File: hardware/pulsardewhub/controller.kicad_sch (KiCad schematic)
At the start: 9 parts, among them J1 SWD, U1 STM32G0B1KBU6, U2 SHT40-AD1B-R2

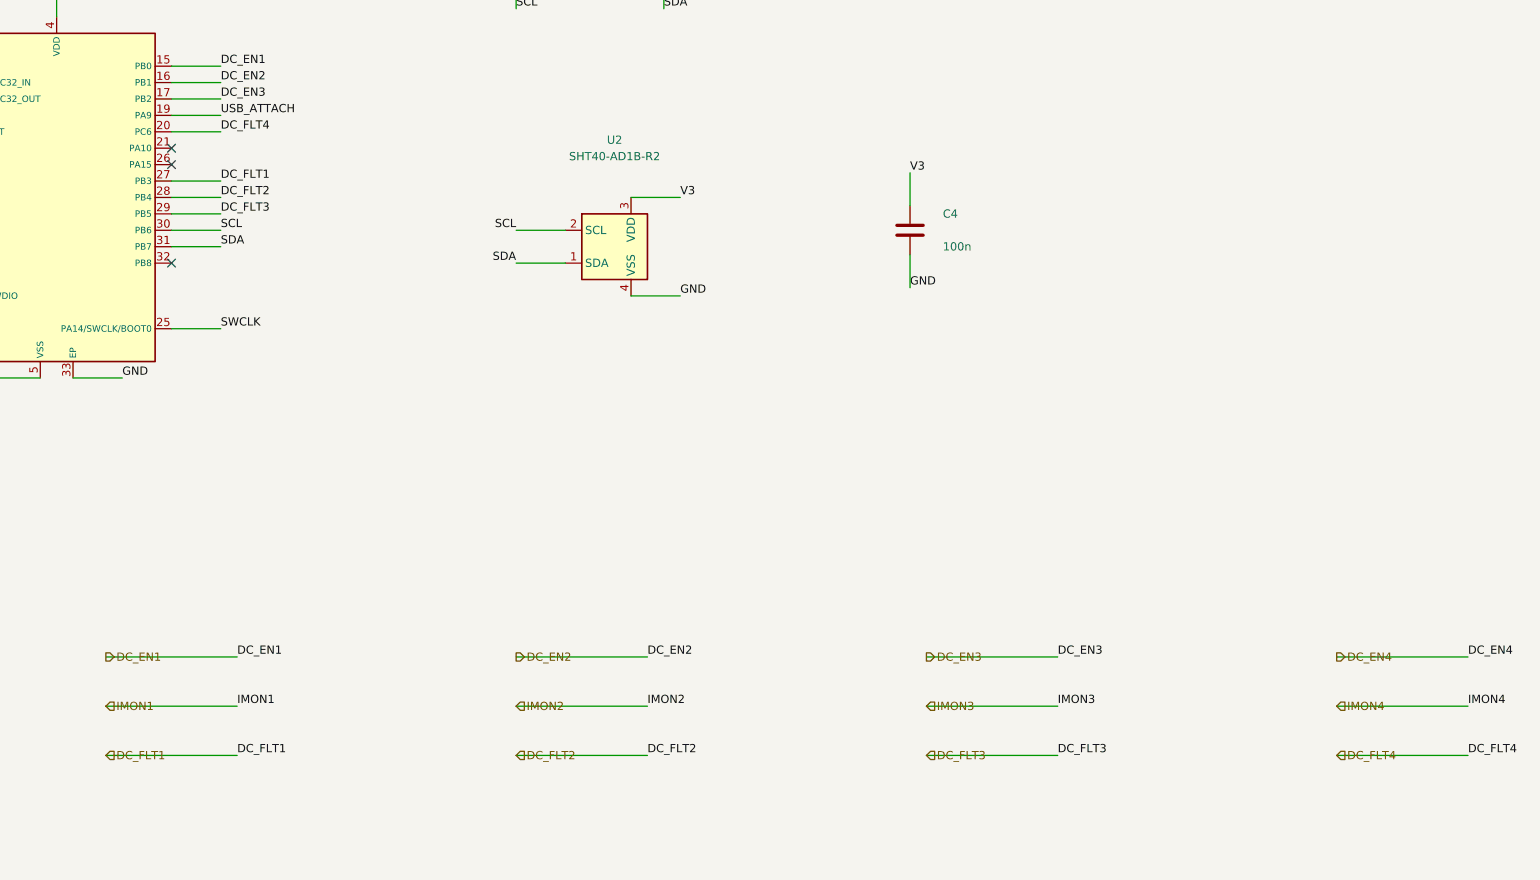
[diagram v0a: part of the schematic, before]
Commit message: Use TPS259827 high-side switches for 12–18 V DC outlets
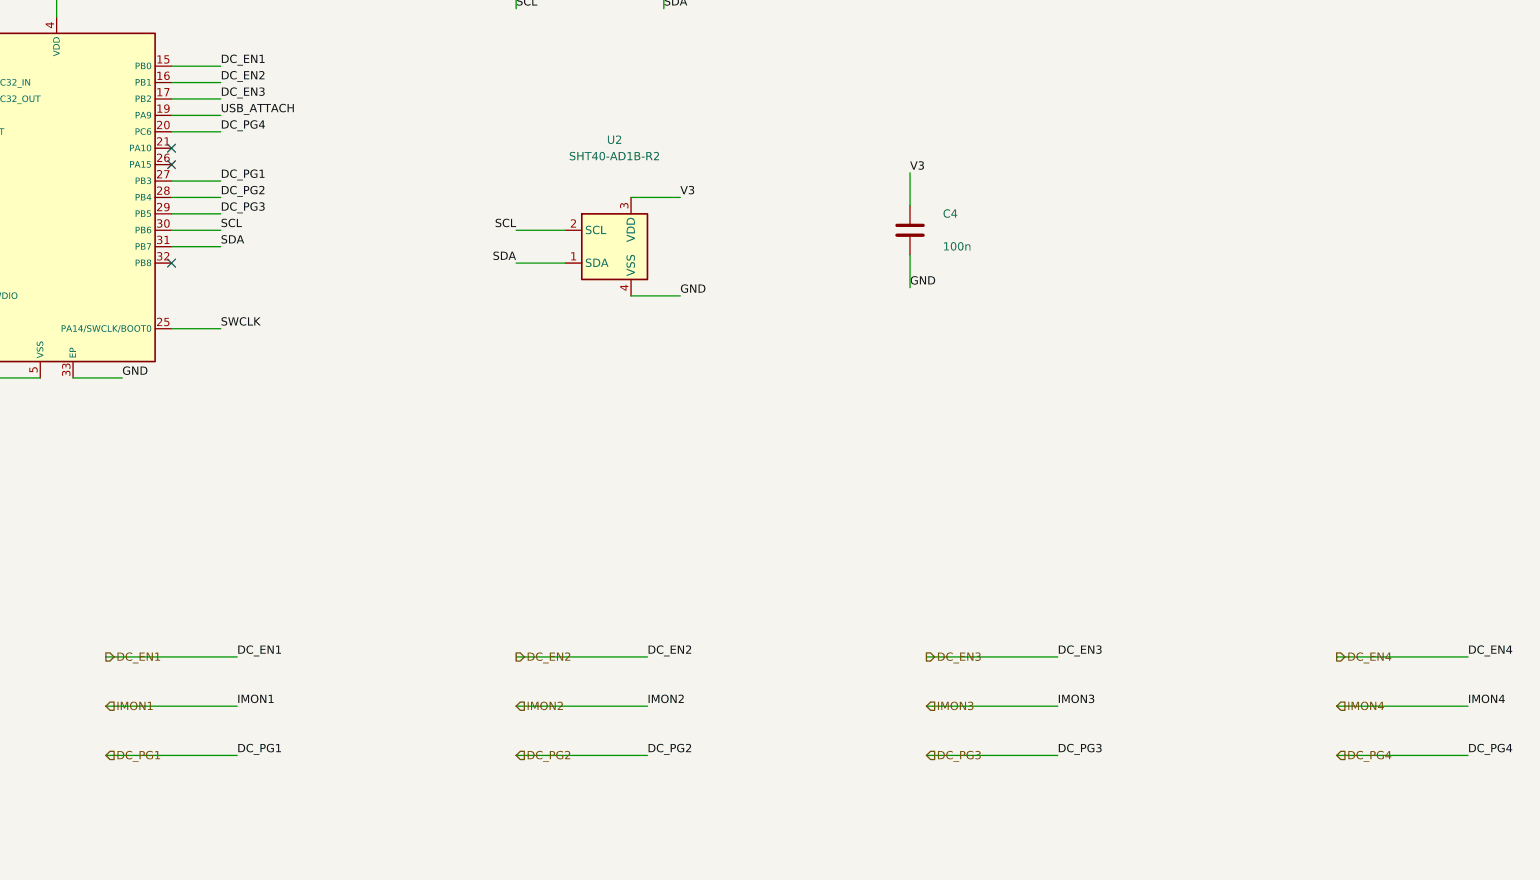
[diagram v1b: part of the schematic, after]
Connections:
- net DC_FLT1 renamed DC_PG1
- net DC_FLT2 renamed DC_PG2
- net DC_FLT3 renamed DC_PG3
- net DC_FLT4 renamed DC_PG4
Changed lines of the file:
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@@
 (kicad_sch (version 20260306) (generator "eeschema") (generator_version "10.0") (paper "A3")
-(title_block (title "PulsarDew Hub - STM32 controller and ambient sensor") (date "2026-10-03") (rev "0.1-draft") (company "PulsarFab"))
+(title_block (title "PulsarDew Hub - STM32 controller and ambient sensor") (date "2026-10-03") (rev "0.2-draft") (company "PulsarFab"))
 (text "CONTROLLER | 2 heater PWM + 4 DC enables / ADC current readings / faults" (at 20.3200 16.5100 0) (effects (font (size 2 2)) (justify left top)))
 (symbol
@@
 (label "DC_EN3"  (at 157.4800 71.1200 0) (effects (font (size 1.27 1.27)) (justify left bottom)))
 (label "DC_EN4"  (at 106.6800 66.0400 180) (effects (font (size 1.27 1.27)) (justify right bottom)))
-(label "DC_FLT1"  (at 157.4800 83.8200 0) (effects (font (size 1.27 1.27)) (justify left bottom)))
-(label "DC_FLT2"  (at 157.4800 86.3600 0) (effects (font (size 1.27 1.27)) (justify left bottom)))
-(label "DC_FLT3"  (at 157.4800 88.9000 0) (effects (font (size 1.27 1.27)) (justify left bottom)))
-(label "DC_FLT4"  (at 157.4800 76.2000 0) (effects (font (size 1.27 1.27)) (justify left bottom)))
+(label "DC_PG1"  (at 157.4800 83.8200 0) (effects (font (size 1.27 1.27)) (justify left bottom)))
+(label "DC_PG2"  (at 157.4800 86.3600 0) (effects (font (size 1.27 1.27)) (justify left bottom)))
+(label "DC_PG3"  (at 157.4800 88.9000 0) (effects (font (size 1.27 1.27)) (justify left bottom)))
+(label "DC_PG4"  (at 157.4800 76.2000 0) (effects (font (size 1.27 1.27)) (justify left bottom)))
 (label "MCU_DM"  (at 106.6800 104.1400 180) (effects (font (size 1.27 1.27)) (justify right bottom)))
 (label "MCU_DP"  (at 106.6800 106.6800 180) (effects (font (size 1.27 1.27)) (justify right bottom)))
@@
 (hierarchical_label "IMON1" (shape input) (at 139.7000 165.1000 0) (effects (font (size 1.27 1.27)) (justify left bottom)))
 (label "IMON1"  (at 160.0200 165.1000 0) (effects (font (size 1.27 1.27)) (justify left bottom)))
-(hierarchical_label "DC_FLT1" (shape input) (at 139.7000 172.7200 0) (effects (font (size 1.27 1.27)) (justify left bottom)))
-(label "DC_FLT1"  (at 160.0200 172.7200 0) (effects (font (size 1.27 1.27)) (justify left bottom)))
+(hierarchical_label "DC_PG1" (shape input) (at 139.7000 172.7200 0) (effects (font (size 1.27 1.27)) (justify left bottom)))
+(label "DC_PG1"  (at 160.0200 172.7200 0) (effects (font (size 1.27 1.27)) (justify left bottom)))
 (hierarchical_label "DC_EN2" (shape output) (at 203.2000 157.4800 0) (effects (font (size 1.27 1.27)) (justify left bottom)))
 (label "DC_EN2"  (at 223.5200 157.4800 0) (effects (font (size 1.27 1.27)) (justify left bottom)))
 (hierarchical_label "IMON2" (shape input) (at 203.2000 165.1000 0) (effects (font (size 1.27 1.27)) (justify left bottom)))
 (label "IMON2"  (at 223.5200 165.1000 0) (effects (font (size 1.27 1.27)) (justify left bottom)))
-(hierarchical_label "DC_FLT2" (shape input) (at 203.2000 172.7200 0) (effects (font (size 1.27 1.27)) (justify left bottom)))
-(label "DC_FLT2"  (at 223.5200 172.7200 0) (effects (font (size 1.27 1.27)) (justify left bottom)))
+(hierarchical_label "DC_PG2" (shape input) (at 203.2000 172.7200 0) (effects (font (size 1.27 1.27)) (justify left bottom)))
+(label "DC_PG2"  (at 223.5200 172.7200 0) (effects (font (size 1.27 1.27)) (justify left bottom)))
 (hierarchical_label "DC_EN3" (shape output) (at 266.7000 157.4800 0) (effects (font (size 1.27 1.27)) (justify left bottom)))
 (label "DC_EN3"  (at 287.0200 157.4800 0) (effects (font (size 1.27 1.27)) (justify left bottom)))
 (hierarchical_label "IMON3" (shape input) (at 266.7000 165.1000 0) (effects (font (size 1.27 1.27)) (justify left bottom)))
 (label "IMON3"  (at 287.0200 165.1000 0) (effects (font (size 1.27 1.27)) (justify left bottom)))
-(hierarchical_label "DC_FLT3" (shape input) (at 266.7000 172.7200 0) (effects (font (size 1.27 1.27)) (justify left bottom)))
-(label "DC_FLT3"  (at 287.0200 172.7200 0) (effects (font (size 1.27 1.27)) (justify left bottom)))
+(hierarchical_label "DC_PG3" (shape input) (at 266.7000 172.7200 0) (effects (font (size 1.27 1.27)) (justify left bottom)))
+(label "DC_PG3"  (at 287.0200 172.7200 0) (effects (font (size 1.27 1.27)) (justify left bottom)))
 (hierarchical_label "DC_EN4" (shape output) (at 330.2000 157.4800 0) (effects (font (size 1.27 1.27)) (justify left bottom)))
 (label "DC_EN4"  (at 350.5200 157.4800 0) (effects (font (size 1.27 1.27)) (justify left bottom)))
 (hierarchical_label "IMON4" (shape input) (at 330.2000 165.1000 0) (effects (font (size 1.27 1.27)) (justify left bottom)))
 (label "IMON4"  (at 350.5200 165.1000 0) (effects (font (size 1.27 1.27)) (justify left bottom)))
-(hierarchical_label "DC_FLT4" (shape input) (at 330.2000 172.7200 0) (effects (font (size 1.27 1.27)) (justify left bottom)))
-(label "DC_FLT4"  (at 350.5200 172.7200 0) (effects (font (size 1.27 1.27)) (justify left bottom)))
+(hierarchical_label "DC_PG4" (shape input) (at 330.2000 172.7200 0) (effects (font (size 1.27 1.27)) (justify left bottom)))
+(label "DC_PG4"  (at 350.5200 172.7200 0) (effects (font (size 1.27 1.27)) (justify left bottom)))
 (text "PA0/PA1: active-high TIM2 heater drive. PB0/PB1/PB2/PB9: static DC GPIO only (never PWM).\nPA4..PA7: ADC IMON1..4. PB3/PB4/PB5/PC6: active-low DC faults.\nPA9: internal hub port 1 enable (3.3 V). Attach USB only while high; disable UCPD dead-battery pull-down.\nSHT40 at 0x44; keep physically away from power components. New firmware pin map is required." (at 25.4000 223.5200 0) (effects (font (size 1.4 1.4)) (justify left top)))
 (wire (pts (xy 25.4000 147.3200) (xy 45.7200 147.3200)) (stroke (width 0) (type default)))

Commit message: Reduce PulsarPower power-path cost while retaining current monitoring
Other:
- title: PulsarDew Hub - STM32 controller and ambient sensor -> PulsarPower - STM32 controller and ambient sensor
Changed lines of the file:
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@@
 (kicad_sch (version 20260306) (generator "eeschema") (generator_version "10.0") (paper "A3")
-(title_block (title "PulsarDew Hub - STM32 controller and ambient sensor") (date "2026-10-03") (rev "0.2-draft") (company "PulsarFab"))
+(title_block (title "PulsarPower - STM32 controller and ambient sensor") (date "2026-10-03") (rev "0.3-draft") (company "PulsarFab"))
 (text "CONTROLLER | 2 heater PWM + 4 DC enables / ADC current readings / faults" (at 20.3200 16.5100 0) (effects (font (size 2 2)) (justify left top)))
 (symbol
